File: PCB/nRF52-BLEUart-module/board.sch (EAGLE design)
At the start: 2 parts, among them J1 USB-A_PTH_MALE, U1 NRF52832

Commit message: PCB update
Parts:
- added C1: 0402, angrypig7-RCL:C-NON-POLC0402
- added C10: 2.2uF, angrypig7-RCL:C-NON-POLC0603
- added C11, C13, C14, C15, C4, C6: 100nF, angrypig7-RCL:C-NON-POLC0402
- added C12: 4.7uF, angrypig7-RCL:C-NON-POLC0402
- added C16, C17, C7, C8: 12pF, angrypig7-RCL:C-NON-POLC0402
- added C2: 0603, angrypig7-RCL:C-NON-POLC0603
- added C3: 0805, angrypig7-RCL:C-NON-POLC0805
- added C5: 10uF, angrypig7-RCL:C-NON-POLC0603
- added C9: 1uF, angrypig7-RCL:C-NON-POLC0402
- added D1: B5819W, angrypig7-Diodes:DIODE-SCHOTTKY_SOD-123
- added JP1: (no value), angrypig7-Connectors-PinHeads:PINHD-1X4
- added TC1: TC2030-IDC-NL, angrypig7-Connectors-Programming:TC2030-IDC-NL
- added TP1: TEST-POINT-3, angrypig7-Tests:TEST-POINT-3
- added VR1: AP2210K-3.3TRG, angrypig7-IC-Power:AP2210K
- added Y1: 32.768kHz, angrypig7-Clocks:CRYSTAL-32.768KHZ_3215
- added Y2: 32MHz_2016, angrypig7-Clocks:CRYSTAL-2.0X1.6MM
- J1: LCSC (none) -> C98125
- U1: LCSC (none) -> C77540
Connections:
- new net 3V3: C10.1, C12.1, C14.1, C15.1, TC1.VREF, TP1.2, U1.VDD@0, U1.VDD@1, U1.VDD@2, VR1.VOUT
- new net 5V: C9.1, D1.C, TP1.3, VR1.EN, VR1.VIN
- new net GND: C10.2, C11.2, C12.2, C13.2, C14.2, C15.2, C16.2, C17.2, C4.2, C6.2, C7.1, C8.1, C9.2, J1.GND, J1.SHIELD, TC1.GND, TP1.1, U1.VSS@1, VR1.GND, Y2.GND
- new net N$1: C8.2, U1.P0.00.XL1, Y1.2
- new net N$2: C4.1, D1.A, J1.VBUS
- new net N$3: C6.1, VR1.BYP/ADJ
- new net N$4: C7.2, U1.P0.01/XL2, Y1.1
- new net N$5: C11.1, U1.DEC1
- new net N$6: U1.ANT
- new net N$7: C13.1, U1.DEC4
- new net N$8: C17.1, U1.XC2, Y2.2
- new net N$9: C16.1, U1.XC1, Y2.1
- new net NRST: TC1.RST, U1.P0.21/NRST
- new net SWDCLK: TC1.TCK, U1.SWDCLK
- new net SWDIO: TC1.TMS, U1.SWDIO
- new net SWO: TC1.TDO, U1.P0.18/TRACED0/SWO
- new net USB_D_N: J1.D-
- new net USB_D_P: J1.D+
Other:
- moved on the sheet: J1, U1

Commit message: PCB update
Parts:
- added D2: TVS, angrypig7-Diodes:TVS-ARRAY_SOT-23-6
- added D3, D4, D5, D6: 0603, angrypig7-Diodes:LED_0603
- added L1: (no value), angrypig7-RCL:L0402
- added R1, R2, R3, R4, R5: 10k, angrypig7-RCL:RR0402
- added S1: SPST-3x4mm, angrypig7-Switches:SWITCH-SPST-SMD-3.0X4.0MM
- added U2: NRF52832, angrypig7-IC-MCU:NRF52832
- C1: value 0402 -> 1uF; LCSC (none) -> C52923
- C10: value 2.2uF -> 100nF; device angrypig7-RCL:C-NON-POLC0603 -> angrypig7-RCL:C-NON-POLC0402; LCSC C23630 -> C1525
- C11, C6: value 100nF -> 12pF; LCSC C1525 -> C1547
- C12: value 4.7uF -> 100nF; LCSC C23733 -> C1525
- C13: value 100nF -> 100pF; LCSC C1525 -> C1546
- C14: value 100nF -> 1uF; LCSC C1525 -> C52923
- C15: value 100nF -> 0.8pF
- C16: value 12pF -> 0.8pF; LCSC C1547 -> C1525
- C17: value 12pF -> 100nF; LCSC C1547 -> C1525
- C2: value 0603 -> 2.2uF; LCSC (none) -> C23630
- C3: value 0805 -> 100nF; device angrypig7-RCL:C-NON-POLC0805 -> angrypig7-RCL:C-NON-POLC0402; LCSC (none) -> C1525
- C5: value 10uF -> 4.7uF; device angrypig7-RCL:C-NON-POLC0603 -> angrypig7-RCL:C-NON-POLC0402; LCSC C19702 -> C23733
- C9: value 1uF -> 100nF; LCSC C52923 -> C1525
- JP1: value (none) -> V G Rx Tx; device angrypig7-Connectors-PinHeads:PINHD-1X4 -> angrypig7-Connectors-PinHeads:PINHD-1X4/90
- U1: value NRF52832 -> CH340E; device angrypig7-IC-MCU:NRF52832 -> angrypig7-IC:CH340E; LCSC C77540 -> C99652
- Y1: value 32.768kHz -> 32MHz_2016; device angrypig7-Clocks:CRYSTAL-32.768KHZ_3215 -> angrypig7-Clocks:CRYSTAL-2.0X1.6MM; LCSC C32346 -> C255896
- Y2: value 32MHz_2016 -> 32.768kHz; device angrypig7-Clocks:CRYSTAL-2.0X1.6MM -> angrypig7-Clocks:CRYSTAL-32.768KHZ_3215; LCSC (none) -> C32346
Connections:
- removed net USB_D_N: J1.D-
- removed net USB_D_P: J1.D+
- new net N$10: C13.1, U2.DEC3
- new net N$11: U2.DEC2
- new net N$12: D4.A, R3.1
- new net N$13: D5.A, R4.1
- new net N$14: D6.A, R5.1
- new net RF-1: C15.1, L1.1, U2.ANT
- new net RF-2: C16.1, L1.2
- new net UART_RX: JP1.4, U1.RX
- new net UART_TX: JP1.3, U1.TX
- new net USB_N: D2.IO3, D2.IO4, J1.D-, U1.UD-
- new net USB_P: D2.IO1, D2.IO2, J1.D+, U1.UD+
- net 3V3: now also C17.1, C2.1, C5.1, C9.1, JP1.1, R1.2, R2.2, R3.2, R4.2, R5.2, U1.V3, U1.VCC, U2.VDD@0, U2.VDD@1, U2.VDD@2; no longer C10.1, C14.1, C15.1, U1.VDD@0, U1.VDD@1, U1.VDD@2
- net 5V: now also C1.1; no longer C9.1
- net GND: now also C1.2, C2.2, C3.2, C5.2, D2.VSS, D3.C, JP1.2, S1.1, U1.GND, U2.PAD, U2.VSS@0, U2.VSS@1, Y1.GND; no longer U1.VSS@1, Y2.GND
- net N$1: now also U2.P0.00.XL1, Y2.2; no longer U1.P0.00.XL1, Y1.2
- net N$2: now also D2.VCC; no longer C4.1
- net N$3: now also C3.1; no longer C6.1
- net N$4: now also U2.P0.01/XL2, Y2.1; no longer U1.P0.01/XL2, Y1.1
- net N$5: now also C10.1, U2.DEC1; no longer C11.1, U1.DEC1
- net N$6: now also D3.A, R1.1; no longer U1.ANT
- net N$7: now also C4.1, U2.DEC4; no longer C13.1, U1.DEC4
- net N$8: now also C6.1, U2.XC2, Y1.2; no longer C17.1, U1.XC2, Y2.2
- net N$9: now also C11.1, U2.XC1, Y1.1; no longer C16.1, U1.XC1, Y2.1
- net NRST: now also C14.1, R2.1, S1.2, U2.P0.21/NRST; no longer U1.P0.21/NRST
- net SWDCLK: now also U2.SWDCLK; no longer U1.SWDCLK
- net SWDIO: now also U2.SWDIO; no longer U1.SWDIO
- net SWO: now also U2.P0.18/TRACED0/SWO; no longer U1.P0.18/TRACED0/SWO

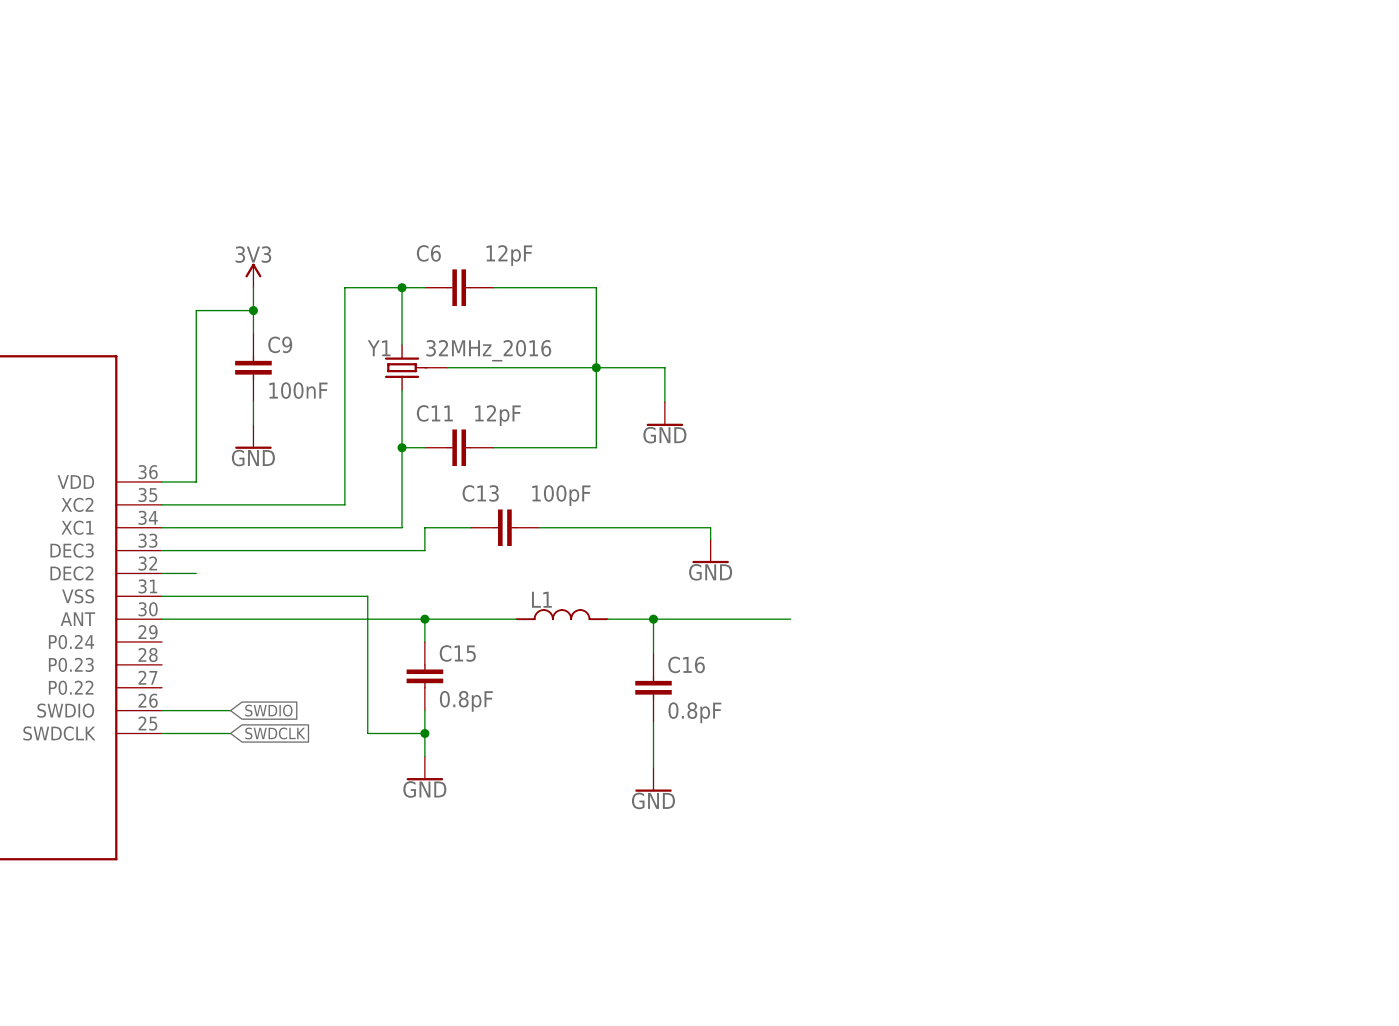
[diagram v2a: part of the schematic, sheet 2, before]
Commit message: PCB update with inverted F antenna
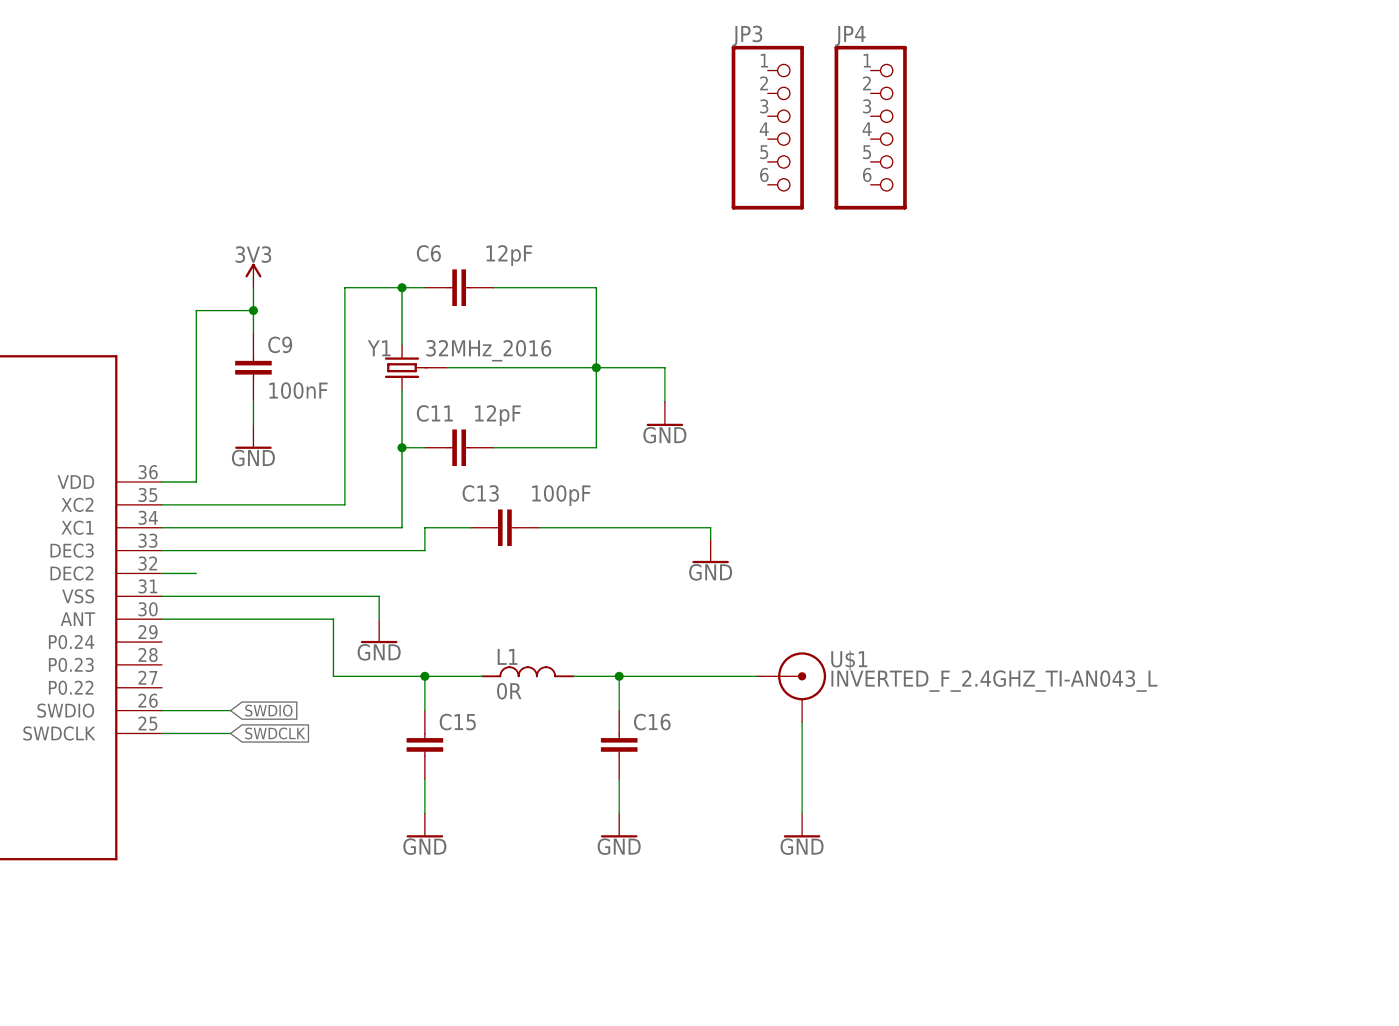
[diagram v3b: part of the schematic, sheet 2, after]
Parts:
- added C18: 100nF, angrypig7-RCL:C-NON-POLC0402
- added JP2: 5V 3V3, angrypig7-Jumpers:JUMPER-SMT_3_1-NC_TRACE_NO-SILK
- added JP3, JP4: (no value), angrypig7-Connectors-PinHeads:PINHD-1X6
- added U$1: INVERTED_F_2.4GHZ_TI-AN043_L, angrypig7-Antennas:INVERTED_F_2.4GHZ_TI-AN043_L
- C15, C16: value 0.8pF -> (none); LCSC C1525 -> (none)
- D3: value 0603 -> PWR
- L1: value (none) -> 0R; LCSC (none) -> C17168
- U2: JLC_ROTATION (none) -> 180
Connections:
- new net N$15: C12.1, JP2.2, U1.VCC
- new net N$16: C18.1, U1.V3
- net 3V3: now also JP2.3; no longer C12.1, U1.V3, U1.VCC
- net 5V: now also JP2.1
- net GND: now also C18.2, U$1.GND
- net RF-2: now also U$1.FEED
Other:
- moved on the sheet: C15, C16, L1

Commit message: artwork partially done, layout update
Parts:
- added C19: TP, angrypig7-RCL:C-NON-POLC0603
- JP1: value V G Rx Tx -> V G Tx Rx
- JP3, JP4: device angrypig7-Connectors-PinHeads:PINHD-1X6 -> angrypig7-Connectors-PinHeads:PINHD-1X5-NOSILK
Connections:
- net N$2 renamed USB_IN
- removed net N$15: C12.1, JP2.2, U1.VCC
- new net VCCIO: C12.1, JP1.1, JP2.2, U1.VCC
- net 3V3: no longer JP1.1
- net GND: now also C19.2
- net RF-1: now also C19.1
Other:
- moved on the sheet: C12, C15, C16, D2, JP2, L1

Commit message: finished PCB artwork
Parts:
- removed C19: TP, angrypig7-RCL:C-NON-POLC0603
- JP2: value 5V 3V3 -> 3V3 5V
- U$1: value INVERTED_F_2.4GHZ_TI-AN043_L -> ANT
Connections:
- removed net N$13: D5.A, R4.1
- new net LED1: R3.1, U2.P0.14/TRACED3
- new net LED2: R4.1, U2.P0.15/TRACED2
- new net LED3: R5.1, U2.P0.16/TRACED1
- new net N$2: D4.A, R3.2
- new net P0.02: JP4.2, U2.P0.02/AIN0
- new net P0.03: JP4.3, U2.P0.03/AIN1
- new net P0.04: JP4.4, U2.P0.04/AIN2
- new net P0.05: JP4.5, U2.P0.05/AIN3
- new net P0.28: JP3.5, U2.P0.28/AIN4
- new net P0.29: JP3.4, U2.P0.29/AIN5
- new net P0.30: JP3.3, U2.P0.30/AIN6
- new net P0.31: JP3.2, U2.P0.31/AIN7
- net 3V3: now also JP2.1, JP3.1; no longer JP2.3, R3.2, R4.2, R5.2
- net 5V: now also JP2.3; no longer JP2.1
- net GND: now also D4.C, D5.C, D6.C, JP4.1; no longer C19.2
- net N$12: now also D5.A, R4.2; no longer D4.A, R3.1
- net N$14: now also R5.2; no longer R5.1
- net RF-1: no longer C19.1
- net UART_RX: now also U1.TX, U2.P.08; no longer U1.RX
- net UART_TX: now also U1.RX, U2.P0.06; no longer U1.TX
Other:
- moved on the sheet: C10, C11, C13, C14, C15, C16, C17, C4, C5, C6, C7, C8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

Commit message: PCB bug fixes, added production files
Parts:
- D3: LCSC (none) -> C2286
- D4, D5, D6: LCSC (none) -> C72038
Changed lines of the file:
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@@
 <part name="GND2" library="angrypig7-Symbols" deviceset="GND" device=""/>
 <part name="GND3" library="angrypig7-Symbols" deviceset="GND" device=""/>
-<part name="U2" library="angrypig7-IC-MCU" deviceset="NRF52832" device="" package3d_urn="urn:adsk.eagle:package:25776865/3">
+<part name="U2" library="angrypig7-IC-MCU" deviceset="NRF52832" device="" package3d_urn="urn:adsk.eagle:package:25776865/5">
 <attribute name="JLC_ROTATION" value="180"/>
 <attribute name="LCSC" value="C77540"/>
@@
 <part name="GND9" library="angrypig7-Symbols" deviceset="GND" device=""/>
 <part name="SUPPLY6" library="angrypig7-Symbols" deviceset="3V3" device=""/>
-<part name="VR1" library="angrypig7-IC-Power" deviceset="AP2210K" device="" package3d_urn="urn:adsk.eagle:package:25814432/6" value="AP2210K-3.3TRG">
+<part name="VR1" library="angrypig7-IC-Power" deviceset="AP2210K" device="" package3d_urn="urn:adsk.eagle:package:25814432/8" value="AP2210K-3.3TRG">
 <attribute name="LCSC" value="C176959"/>
 </part>
@@
 <attribute name="LCSC" value="C25744"/>
 </part>
-<part name="U1" library="angrypig7-IC" deviceset="CH340E" device="" package3d_urn="urn:adsk.eagle:package:25892162/7">
+<part name="U1" library="angrypig7-IC" deviceset="CH340E" device="" package3d_urn="urn:adsk.eagle:package:25892162/9">
 <attribute name="LCSC" value="C99652"/>
 </part>
@@
 <attribute name="LCSC" value="C25744"/>
 </part>
-<part name="D3" library="angrypig7-Diodes" deviceset="LED" device="_0603" package3d_urn="urn:adsk.eagle:package:22866870/2" value="PWR"/>
+<part name="D3" library="angrypig7-Diodes" deviceset="LED" device="_0603" package3d_urn="urn:adsk.eagle:package:22866870/2" value="PWR">
+<attribute name="LCSC" value="C2286"/>
+</part>
 <part name="GND26" library="angrypig7-Symbols" deviceset="GND" device=""/>
-<part name="D2" library="angrypig7-Diodes" deviceset="TVS-ARRAY" device="_SOT-23-6" package3d_urn="urn:adsk.eagle:package:25892184/7" value="TVS">
+<part name="D2" library="angrypig7-Diodes" deviceset="TVS-ARRAY" device="_SOT-23-6" package3d_urn="urn:adsk.eagle:package:25892184/9" value="TVS">
 <attribute name="LCSC" value="C85364"/>
 </part>
@@
 <attribute name="LCSC" value="C25744"/>
 </part>
-<part name="D4" library="angrypig7-Diodes" deviceset="LED" device="_0603" package3d_urn="urn:adsk.eagle:package:22866870/2" value="0603"/>
+<part name="D4" library="angrypig7-Diodes" deviceset="LED" device="_0603" package3d_urn="urn:adsk.eagle:package:22866870/2" value="0603">
+<attribute name="LCSC" value="C72038"/>
+</part>
 <part name="R4" library="angrypig7-RCL" deviceset="R" device="R0402" package3d_urn="urn:adsk.eagle:package:23547/3" value="10k">
 <spice>
@@
 <attribute name="LCSC" value="C25744"/>
 </part>
-<part name="D5" library="angrypig7-Diodes" deviceset="LED" device="_0603" package3d_urn="urn:adsk.eagle:package:22866870/2" value="0603"/>
+<part name="D5" library="angrypig7-Diodes" deviceset="LED" device="_0603" package3d_urn="urn:adsk.eagle:package:22866870/2" value="0603">
+<attribute name="LCSC" value="C72038"/>
+</part>
 <part name="FRAME2" library="angrypig7-Frames" deviceset="FRAME-A3L" device=""/>
 <part name="FRAME1" library="angrypig7-Frames" deviceset="FRAME-A3L" device=""/>
@@
 <attribute name="LCSC" value="C25744"/>
 </part>
-<part name="D6" library="angrypig7-Diodes" deviceset="LED" device="_0603" package3d_urn="urn:adsk.eagle:package:22866870/2" value="0603"/>
+<part name="D6" library="angrypig7-Diodes" deviceset="LED" device="_0603" package3d_urn="urn:adsk.eagle:package:22866870/2" value="0603">
+<attribute name="LCSC" value="C72038"/>
+</part>
 <part name="GND32" library="angrypig7-Symbols" deviceset="GND" device=""/>
 <part name="SUPPLY16" library="angrypig7-Symbols" deviceset="3V3" device=""/>
@@
 <attribute name="NAME" x="274.066" y="184.658" size="1.778" layer="95" rot="R90"/>
 <attribute name="VALUE" x="276.225" y="184.658" size="1.778" layer="96" rot="R90"/>
+<attribute name="LCSC" x="270.51" y="187.96" size="1.27" layer="96" rot="R90" display="off"/>
 </instance>
 <instance part="GND26" gate="1" x="270.51" y="180.34" smashed="yes">
@@
 <attribute name="NAME" x="366.522" y="176.276" size="1.778" layer="95" rot="R180"/>
 <attribute name="VALUE" x="366.522" y="178.435" size="1.778" layer="96" rot="R180"/>
+<attribute name="LCSC" x="363.22" y="172.72" size="1.27" layer="96" rot="R180" display="off"/>
 </instance>
 <instance part="R4" gate="G$1" x="350.52" y="160.02" smashed="yes">
@@
 <attribute name="NAME" x="366.522" y="163.576" size="1.778" layer="95" rot="R180"/>
 <attribute name="VALUE" x="366.522" y="165.735" size="1.778" layer="96" rot="R180"/>
+<attribute name="LCSC" x="363.22" y="160.02" size="1.27" layer="96" rot="R180" display="off"/>
 </instance>
 <instance part="TC1" gate="A" x="351.79" y="86.36" smashed="yes">
@@
 <attribute name="NAME" x="366.522" y="150.876" size="1.778" layer="95" rot="R180"/>
 <attribute name="VALUE" x="366.522" y="153.035" size="1.778" layer="96" rot="R180"/>
+<attribute name="LCSC" x="363.22" y="147.32" size="1.27" layer="96" rot="R180" display="off"/>
 </instance>
 <instance part="GND32" gate="1" x="372.11" y="143.51" smashed="yes">

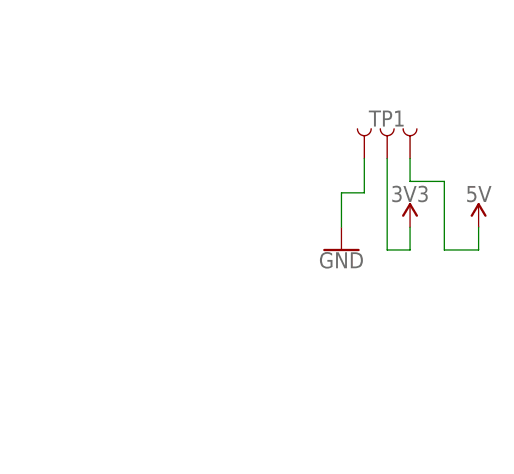
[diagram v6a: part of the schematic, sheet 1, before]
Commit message: fixed #2, removed unecessary power test pad
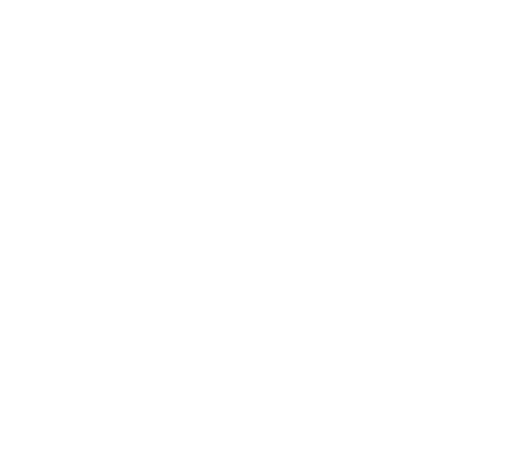
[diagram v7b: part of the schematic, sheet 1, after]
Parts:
- removed TP1: TEST-POINT-3, angrypig7-Tests:TEST-POINT-3
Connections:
- net 3V3: no longer TP1.2
- net 5V: no longer TP1.3
- net GND: no longer TP1.1
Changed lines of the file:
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@@
 <attribute name="LCSC" value="C23630"/>
 </part>
-<part name="TP1" library="angrypig7-Tests" deviceset="TEST-POINT-3" device=""/>
-<part name="SUPPLY7" library="angrypig7-Symbols" deviceset="3V3" device=""/>
-<part name="GND10" library="angrypig7-Symbols" deviceset="GND" device=""/>
-<part name="SUPPLY8" library="angrypig7-Symbols" deviceset="5V" device=""/>
 <part name="Y2" library="angrypig7-Clocks" deviceset="CRYSTAL-32.768KHZ" device="_3215" package3d_urn="urn:adsk.eagle:package:6644366/3" value="32.768kHz">
 <attribute name="LCSC" value="C32346"/>
@@
 <attribute name="VALUE" x="256.794" y="197.231" size="1.778" layer="96"/>
 <attribute name="LCSC" x="255.27" y="200.66" size="1.27" layer="96" display="off"/>
-</instance>
-<instance part="TP1" gate="G$1" x="328.93" y="204.47" smashed="yes">
-<attribute name="NAME" x="328.93" y="205.486" size="1.778" layer="95" font="vector" align="bottom-center"/>
-</instance>
-<instance part="SUPPLY7" gate="G$1" x="331.47" y="194.31" smashed="yes">
-<attribute name="VALUE" x="331.47" y="197.104" size="1.778" layer="96" align="bottom-center"/>
-</instance>
-<instance part="GND10" gate="1" x="323.85" y="194.31" smashed="yes">
-<attribute name="VALUE" x="323.85" y="191.516" size="1.778" layer="96" align="top-center"/>
-</instance>
-<instance part="SUPPLY8" gate="G$1" x="339.09" y="194.31" smashed="yes">
-<attribute name="VALUE" x="339.09" y="197.104" size="1.778" layer="96" align="bottom-center"/>
 </instance>
 <instance part="U1" gate="G$1" x="166.37" y="124.46" smashed="yes">
@@
 </segment>
 <segment>
-<pinref part="GND10" gate="1" pin="GND"/>
-<wire x1="323.85" y1="194.31" x2="323.85" y2="198.12" width="0.1524" layer="91"/>
-<wire x1="323.85" y1="198.12" x2="326.39" y2="198.12" width="0.1524" layer="91"/>
-<pinref part="TP1" gate="G$1" pin="1"/>
-<wire x1="326.39" y1="198.12" x2="326.39" y2="201.93" width="0.1524" layer="91"/>
-</segment>
-<segment>
 <pinref part="GND23" gate="1" pin="GND"/>
 <pinref part="U1" gate="G$1" pin="GND"/>
@@
 </segment>
 <segment>
-<pinref part="TP1" gate="G$1" pin="3"/>
-<wire x1="331.47" y1="201.93" x2="331.47" y2="199.39" width="0.1524" layer="91"/>
-<wire x1="331.47" y1="199.39" x2="335.28" y2="199.39" width="0.1524" layer="91"/>
-<wire x1="335.28" y1="199.39" x2="335.28" y2="191.77" width="0.1524" layer="91"/>
-<pinref part="SUPPLY8" gate="G$1" pin="5V"/>
-<wire x1="335.28" y1="191.77" x2="339.09" y2="191.77" width="0.1524" layer="91"/>
-<wire x1="339.09" y1="191.77" x2="339.09" y2="194.31" width="0.1524" layer="91"/>
-</segment>
-<segment>
 <pinref part="SUPPLY20" gate="G$1" pin="5V"/>
 <wire x1="96.52" y1="127" x2="96.52" y2="135.89" width="0.1524" layer="91"/>
@@
 </segment>
 <segment>
-<pinref part="SUPPLY7" gate="G$1" pin="3V3"/>
-<wire x1="331.47" y1="194.31" x2="331.47" y2="191.77" width="0.1524" layer="91"/>
-<pinref part="TP1" gate="G$1" pin="2"/>
-<wire x1="331.47" y1="191.77" x2="328.93" y2="191.77" width="0.1524" layer="91"/>
-<wire x1="328.93" y1="191.77" x2="328.93" y2="201.93" width="0.1524" layer="91"/>
-</segment>
-<segment>
